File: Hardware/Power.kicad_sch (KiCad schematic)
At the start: 48 parts, among them U1 LT1963AEST-3.3#TRPBF, U2 TPS5405DR, U3 TPS2115ADRBR, U4 LT1963AEST-3.3#TRPBF

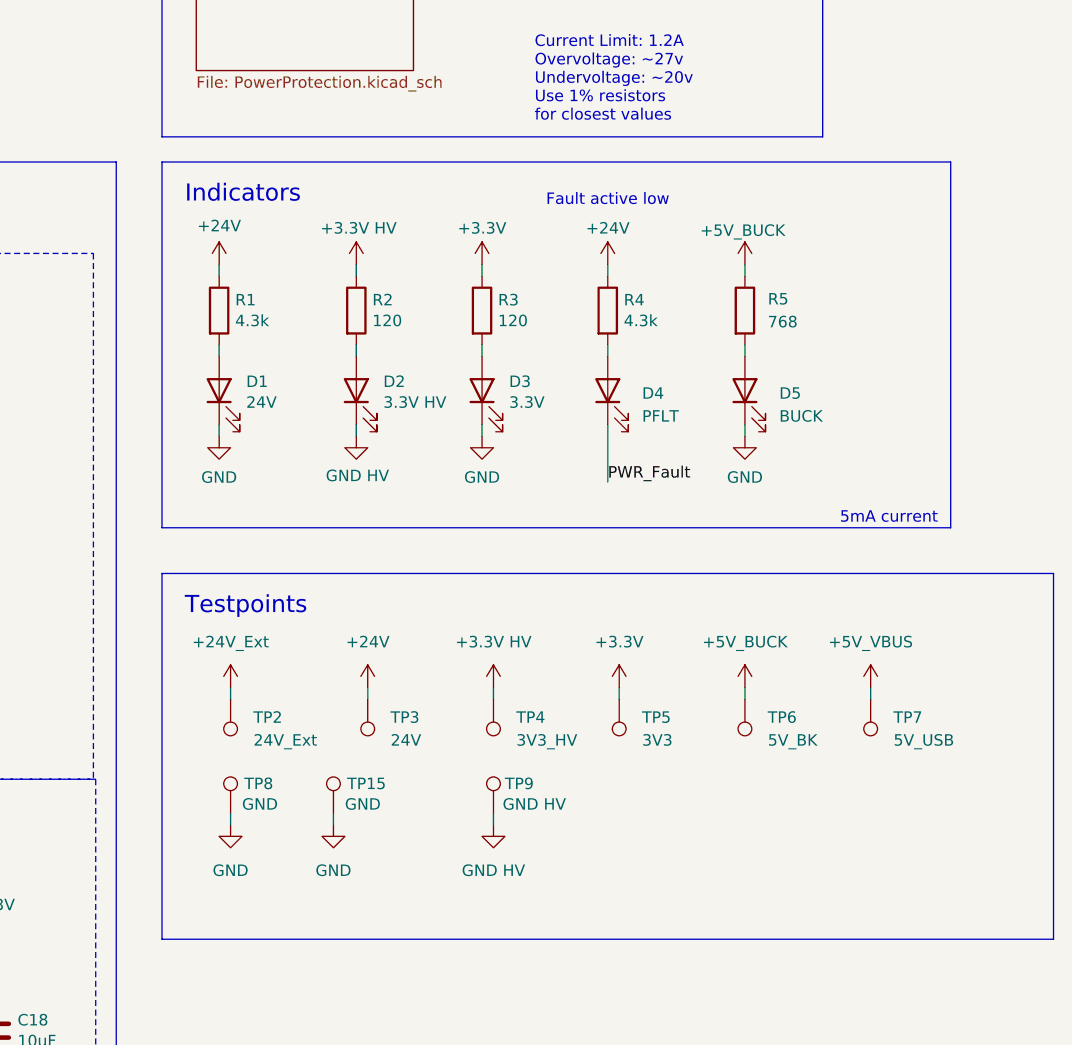
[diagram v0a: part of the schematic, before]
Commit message: added documentation for current range; added VBUS led
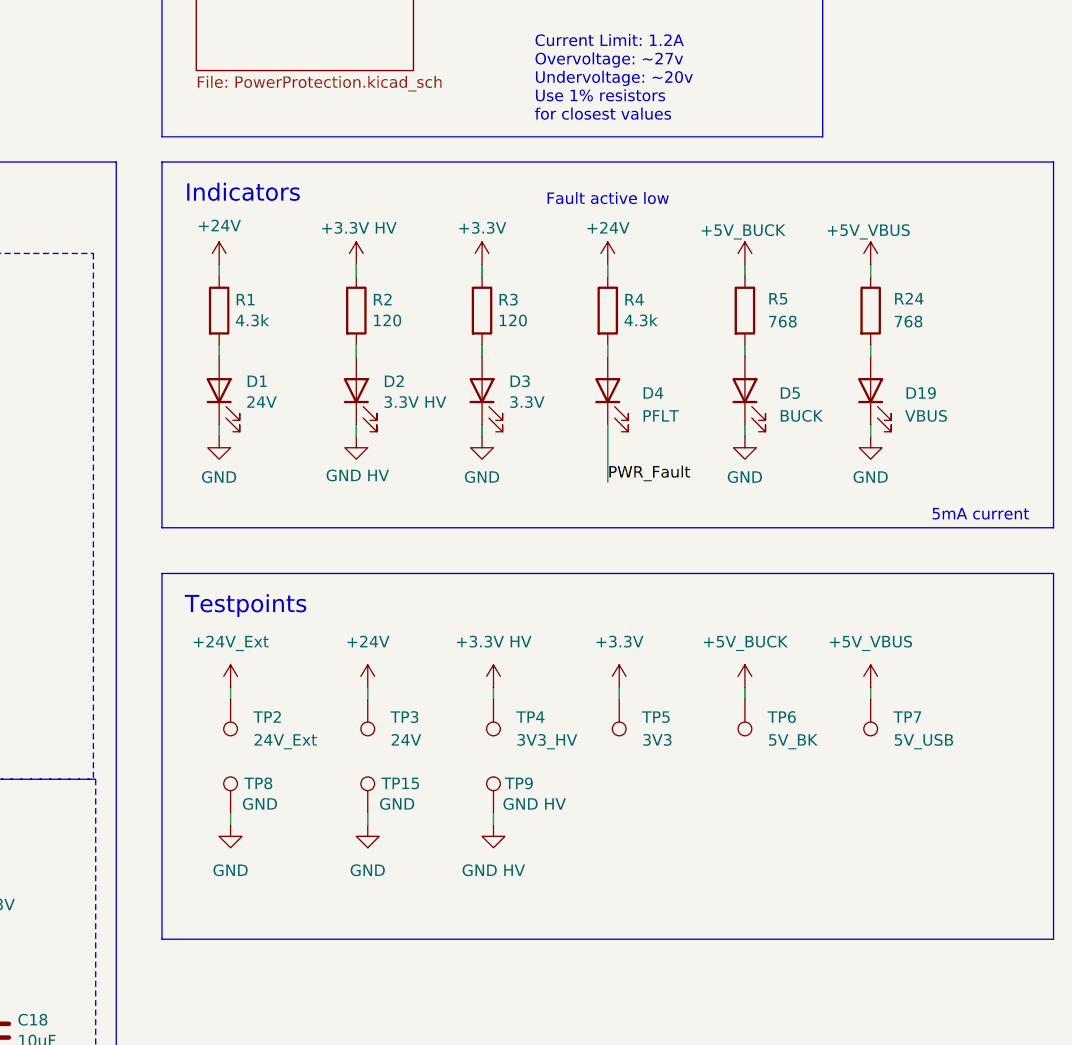
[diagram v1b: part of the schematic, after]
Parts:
- added D19: VBUS, LED_SMD:LED_0603_1608Metric_Pad1.05x0.95mm_HandSolder, symbol Device:LED
- added R24: 768, Resistor_SMD:R_0603_1608Metric_Pad0.98x0.95mm_HandSolder, symbol Device:R
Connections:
- net +5V_VBUS: now also R24.1
- net GND: now also D19.1 (K)
- new net: D19.2 (A), R24.2
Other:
- moved on the sheet: TP15

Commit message: slightly cooked
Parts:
- TP15, TP8, TP9: footprint TestPoint:TestPoint_Pad_1.0x1.0mm -> TestPoint:TestPoint_Pad_1.5x1.5mm
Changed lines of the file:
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@@
 			)
 		)
-		(property "Footprint" "TestPoint:TestPoint_Pad_1.0x1.0mm"
+		(property "Footprint" "TestPoint:TestPoint_Pad_1.5x1.5mm"
 			(at 182.88 138.43 0)
 			(effects
@@
 			)
 		)
-		(property "Footprint" "TestPoint:TestPoint_Pad_1.0x1.0mm"
+		(property "Footprint" "TestPoint:TestPoint_Pad_1.5x1.5mm"
 			(at 198.12 138.43 0)
 			(effects
@@
 			)
 		)
-		(property "Footprint" "TestPoint:TestPoint_Pad_1.0x1.0mm"
+		(property "Footprint" "TestPoint:TestPoint_Pad_1.5x1.5mm"
 			(at 212.09 138.43 0)
 			(effects

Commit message: layout stuff
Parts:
- TP15, TP8, TP9: footprint TestPoint:TestPoint_Pad_1.5x1.5mm -> UTSVT_Special:TestPoint_HEX_3mmID
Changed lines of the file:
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@@
 			)
 		)
-		(property "Footprint" "TestPoint:TestPoint_Pad_1.5x1.5mm"
+		(property "Footprint" "UTSVT_Special:TestPoint_HEX_3mmID"
 			(at 182.88 138.43 0)
 			(effects
@@
 			)
 		)
-		(property "Footprint" "TestPoint:TestPoint_Pad_1.5x1.5mm"
+		(property "Footprint" "UTSVT_Special:TestPoint_HEX_3mmID"
 			(at 198.12 138.43 0)
 			(effects
@@
 			)
 		)
-		(property "Footprint" "TestPoint:TestPoint_Pad_1.5x1.5mm"
+		(property "Footprint" "UTSVT_Special:TestPoint_HEX_3mmID"
 			(at 212.09 138.43 0)
 			(effects

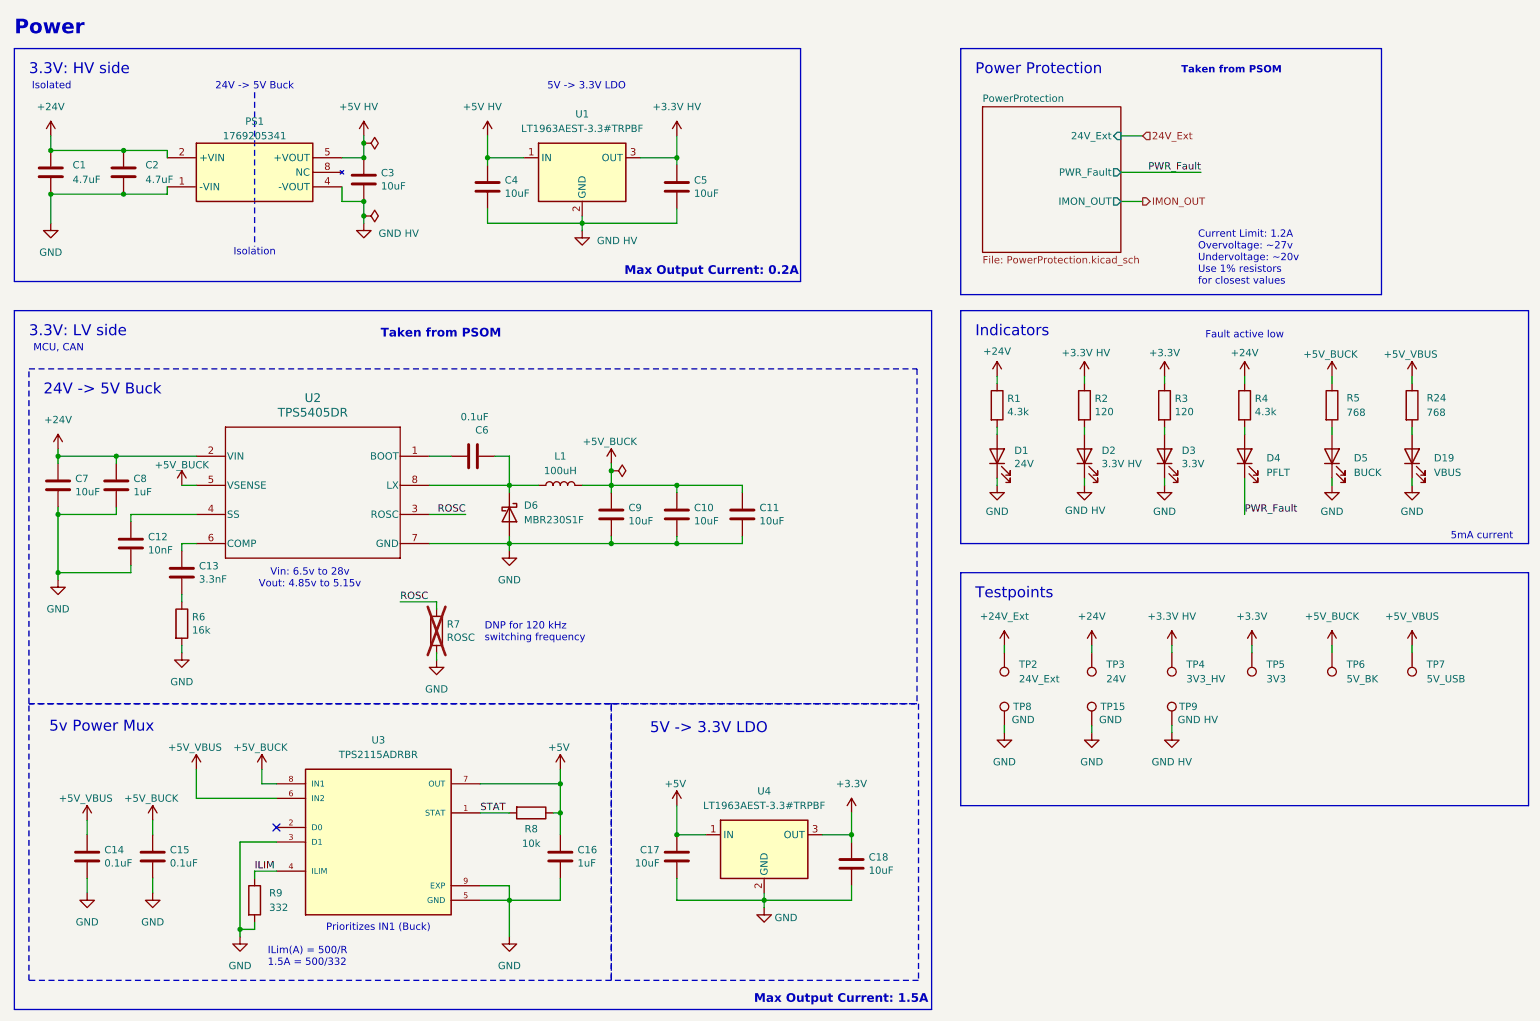
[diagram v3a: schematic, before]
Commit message: post review council sch changes: shielded connectors, removed SHDN resistor, diode OR for boot, standardized resistors
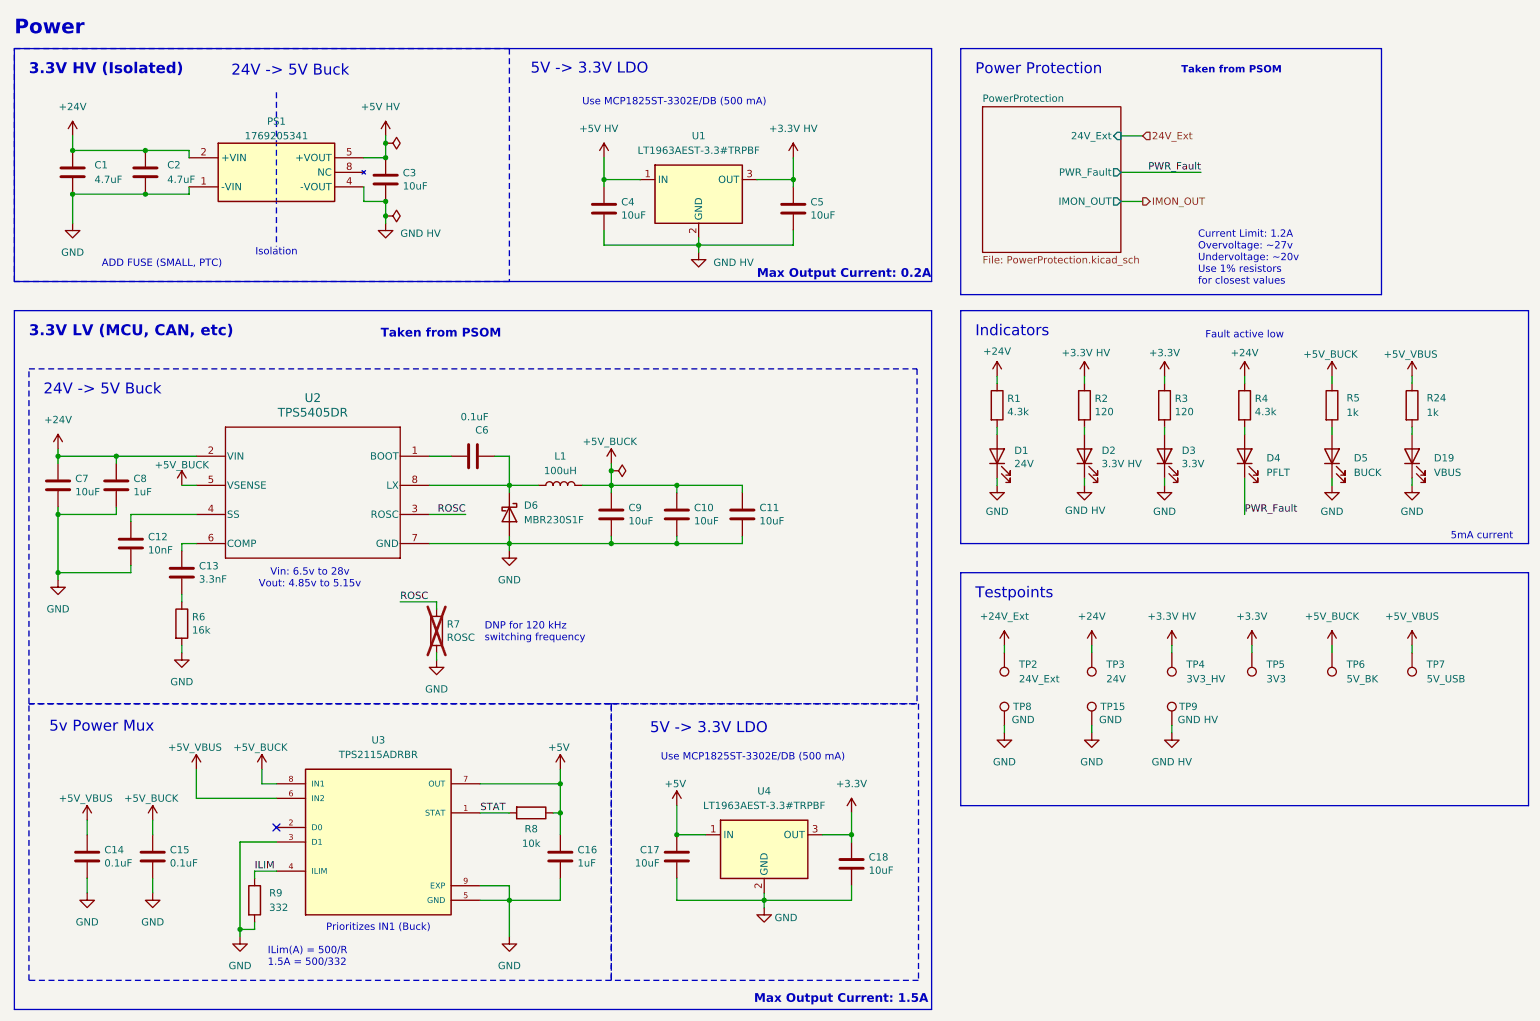
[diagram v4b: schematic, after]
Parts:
- R24, R5: value 768 -> 1k
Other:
- note added: "3.3V HV (Isolated)"
- note added: "3.3V LV (MCU, CAN, etc)"
- note added: "ADD FUSE (SMALL, PTC)"
- note added: "Use MCP1825ST-3302E/DB (500 mA)"
- note removed: "3.3V: HV side"
- note removed: "3.3V: LV side"
- note removed: "Isolated"
- note removed: "MCU, CAN"
- moved on the sheet: C1, C2, C3, C4, C5, PS1, U1

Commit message: almost done with routing
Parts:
- added F1: Fuse, Parts:FUSC3216X125N, symbol Device:Fuse
- added TP21: 5V_HV, TestPoint:TestPoint_Pad_1.0x1.0mm, symbol Connector:TestPoint
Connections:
- net +24V: now also F1.2; no longer C1.1, C2.1, PS1.2 (+VIN)
- net +5V HV: now also TP21.1
- new net: C1.1, C2.1, F1.1, PS1.2 (+VIN)
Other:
- note added: "HV"
- note added: "LV"
- note added: "PTC fuse 30 VDC, 250 mA trip"
- note removed: "ADD FUSE (SMALL, PTC)"
- moved on the sheet: C1, C2, C3, PS1, TP15, TP3, TP4, TP5, TP6, TP7, TP8, TP9

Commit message: addressed some comments
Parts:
- added TP22: 24V_HV, TestPoint:TestPoint_Pad_1.0x1.0mm, symbol Connector:TestPoint
- TP15, TP8, TP9: footprint UTSVT_Special:TestPoint_HEX_3mmID -> Connector_PinHeader_2.54mm:PinHeader_1x01_P2.54mm_Vertical
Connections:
- net at C1.1, C2.1, F1.1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: now also TP22.1
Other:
- note removed: "5mA current"
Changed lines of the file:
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@@
 		)
 	)
-	(text "5mA current"
-		(exclude_from_sim no)
-		(at 271.272 105.41 0)
-		(effects
-			(font
-				(size 1.27 1.27)
-			)
-		)
-	)
 	(text "PTC fuse\n30 VDC, 250 mA trip"
 		(exclude_from_sim no)
@@
 	(wire
 		(pts
+			(xy 25.4 40.64) (xy 29.21 40.64)
+		)
+		(stroke
+			(width 0)
+			(type default)
+		)
+	)
+	(wire
+		(pts
 			(xy 58.42 148.59) (xy 58.42 146.05)
 		)
@@
 			)
 		)
-		(property "Footprint" "UTSVT_Special:TestPoint_HEX_3mmID"
+		(property "Footprint" "Connector_PinHeader_2.54mm:PinHeader_1x01_P2.54mm_Vertical"
 			(at 208.28 139.7 0)
 			(effects
@@
 	(symbol
 		(lib_id "Connector:TestPoint")
+		(at 25.4 40.64 0)
+		(mirror x)
+		(unit 1)
+		(exclude_from_sim no)
+		(in_bom no)
+		(on_board yes)
+		(dnp no)
+		(property "Reference" "TP22"
+			(at 22.86 42.6719 0)
+			(effects
+				(font
+					(size 1.27 1.27)
+				)
+				(justify right)
+			)
+		)
+		(property "Value" "24V_HV"
+			(at 22.86 45.2119 0)
+			(effects
+				(font
+					(size 1.27 1.27)
+				)
+				(justify right)
+			)
+		)
+		(property "Footprint" "TestPoint:TestPoint_Pad_1.0x1.0mm"
+			(at 30.48 40.64 0)
+			(effects
+				(font
+					(size 1.27 1.27)
+				)
+				(hide yes)
+			)
+		)
+		(property "Datasheet" "~"
+			(at 30.48 40.64 0)
+			(effects
+				(font
+					(size 1.27 1.27)
+				)
+				(hide yes)
+			)
+		)
+		(property "Description" "test point"
+			(at 25.4 40.64 0)
+			(effects
+				(font
+					(size 1.27 1.27)
+				)
+				(hide yes)
+			)
+		)
+		(pin "1"
+		)
+		(instances
+			(project "PS-AmperesPCB"
+				(path "/a452d214-ea00-440d-a445-5d6103fda43a/3b2a70f8-48f8-45b9-b0fe-085893d574c0"
+					(reference "TP22")
+					(unit 1)
+				)
+			)
+		)
+	)
+	(symbol
+		(lib_id "Connector:TestPoint")
 		(at 231.14 139.7 0)
 		(mirror y)
@@
 			)
 		)
-		(property "Footprint" "UTSVT_Special:TestPoint_HEX_3mmID"
+		(property "Footprint" "Connector_PinHeader_2.54mm:PinHeader_1x01_P2.54mm_Vertical"
 			(at 226.06 139.7 0)
 			(effects
@@
 			)
 		)
-		(property "Footprint" "UTSVT_Special:TestPoint_HEX_3mmID"
+		(property "Footprint" "Connector_PinHeader_2.54mm:PinHeader_1x01_P2.54mm_Vertical"
 			(at 257.81 139.7 0)
 			(effects
